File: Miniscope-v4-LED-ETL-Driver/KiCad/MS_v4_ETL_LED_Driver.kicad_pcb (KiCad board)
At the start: 4 copper layers, 8 x 10.5 mm, 20 parts, among them J1 Conn_01x01, J10 Conn_01x05, J6 Conn_01x01, J7 Conn_01x01, U1 MAX14574EWL+, U2 TPL0102-100RUCR, U3 LTC3218

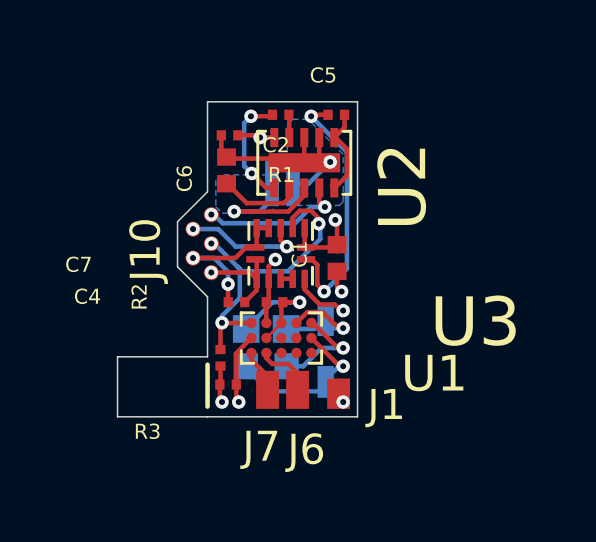
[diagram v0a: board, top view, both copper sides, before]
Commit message: Finalize LED-EWL, MCU, and PYTHON480 PCB for fabrication
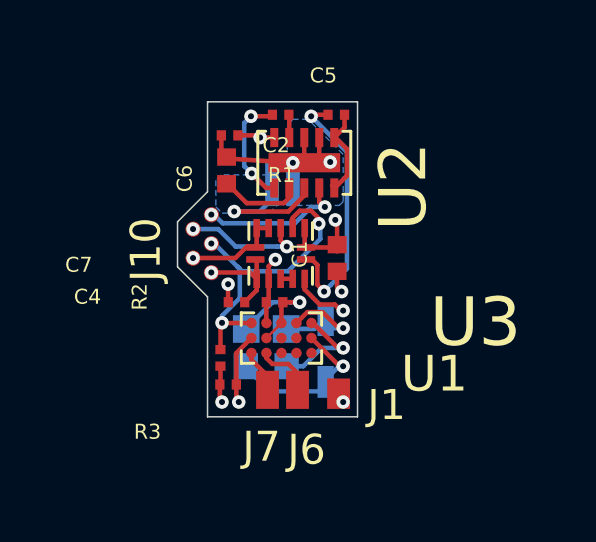
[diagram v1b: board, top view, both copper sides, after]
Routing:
- net GND: track 23.2 -> 22.7 mm, vias 8 -> 9
- added copper zone on In4.Cu, net +3V3
- removed copper zone on In2.Cu, net +3V3
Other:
- board size 8 x 10.5 mm -> 6 x 10.5 mm
- copper layers 4 -> 6
- board text added: "P3"
- board text removed: "P2"
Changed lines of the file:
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@@
-(kicad_pcb (version 20171130) (host pcbnew "(5.0.1)-3")
+(kicad_pcb (version 20171130) (host pcbnew "(5.1.0)-1")
   (general
     (thickness 0.8)
-    (drawings 16)
-    (tracks 211)
+    (drawings 13)
+    (tracks 209)
     (zones 0)
     (modules 20)
@@
     (1 In1.Cu power)
     (2 In2.Cu signal)
+    (3 In3.Cu signal)
+    (4 In4.Cu signal)
     (31 B.Cu signal)
     (32 B.Adhes user)
@@
     (44 Edge.Cuts user)
     (45 Margin user)
-    (46 B.CrtYd user)
-    (47 F.CrtYd user)
+    (46 B.CrtYd user hide)
+    (47 F.CrtYd user hide)
     (48 B.Fab user hide)
     (49 F.Fab user hide)
   )
   (setup
-    (last_trace_width 0.0889)
+    (last_trace_width 0.152)
     (user_trace_width 0.09)
     (user_trace_width 0.1016)
@@
     (zone_45_only yes)
     (trace_min 0.0889)
-    (segment_width 0.2)
-    (edge_width 0.15)
     (via_size 0.45)
     (via_drill 0.2)
@@
     (uvia_min_size 0.2)
     (uvia_min_drill 0.1)
+    (edge_width 0.15)
+    (segment_width 0.2)
     (pcb_text_width 0.3)
     (pcb_text_size 1.5 1.5)
@@
     )
   )
-  (gr_line (start 13.2842 22.0472) (end 13.2842 23.4442) (layer F.SilkS) (width 0.1524))
-  (gr_line (start 10.2842 23.7842) (end 13.2842 23.7842) (layer Edge.Cuts) (width 0.0508))
-  (gr_line (start 10.2842 21.7842) (end 10.2842 23.7842) (layer Edge.Cuts) (width 0.0508))
-  (gr_line (start 13.2842 21.7842) (end 10.2842 21.7842) (layer Edge.Cuts) (width 0.0508))
-  (gr_text P2 (at 15.6718 18.6944) (layer B.SilkS)
+  (gr_line (start 13.2842 21.7842) (end 13.2842 23.7842) (layer Edge.Cuts) (width 0.0508))
+  (gr_text P3 (at 15.6718 18.6944) (layer B.SilkS)
     (effects (font (size 1.5 1.5) (thickness 0.3)) (justify mirror))
   )
@@
   (segment (start 13.97 15.176) (end 13.9192 15.1252) (width 0.152) (layer F.Cu) (net 11))
   (segment (start 16.51 15.3162) (end 16.3698 15.176) (width 0.152) (layer F.Cu) (net 11))
-  (segment (start 16.3698 15.176) (end 13.97 15.176) (width 0.152) (layer F.Cu) (net 11))
+  (segment (start 16.3698 15.176) (end 16.129 15.3162) (width 0.152) (layer F.Cu) (net 11))
   (segment (start 13.7458 14.9518) (end 13.9192 15.1252) (width 0.152) (layer F.Cu) (net 11))
   (segment (start 13.7458 14.4018) (end 13.7458 14.9518) (width 0.152) (layer F.Cu) (net 11))
-  (segment (start 16.6552 16.0092) (end 17.3736 15.2908) (width 0.152) (layer B.Cu) (net 11))
-  (segment (start 16.1342 16.0092) (end 16.6552 16.0092) (width 0.152) (layer B.Cu) (net 11))
   (via (at 17.5425 17.2212) (size 0.45) (drill 0.2) (layers F.Cu B.Cu) (net 11))
   (segment (start 17.6022 18.0462) (end 17.6022 17.2809) (width 0.152) (layer F.Cu) (net 11))
@@
   (segment (start 16.477001 22.098) (end 17.086601 21.4884) (width 0.152) (layer B.Cu) (net 11))
   (segment (start 15.920001 22.098) (end 16.477001 22.098) (width 0.152) (layer B.Cu) (net 11))
-  (segment (start 13.97 18.955546) (end 13.97 19.087402) (width 0.152) (layer B.Cu) (net 11))
-  (segment (start 13.505654 18.4912) (end 13.97 18.955546) (width 0.152) (layer B.Cu) (net 11))
-  (segment (start 12.8016 18.4912) (end 13.505654 18.4912) (width 0.152) (layer B.Cu) (net 11))
   (via (at 13.970001 19.3637) (size 0.45) (drill 0.2) (layers F.Cu B.Cu) (net 11))
-  (segment (start 13.97 19.087402) (end 13.97 19.363699) (width 0.152) (layer B.Cu) (net 11))
   (segment (start 13.97 19.363699) (end 13.970001 19.3637) (width 0.152) (layer B.Cu) (net 11))
   (segment (start 13.970001 19.960001) (end 13.9744 19.9644) (width 0.152) (layer F.Cu) (net 11))
   (segment (start 13.970001 19.3637) (end 13.970001 19.960001) (width 0.152) (layer F.Cu) (net 11))
+  (segment (start 15.494 18.4912) (end 15.5448 18.542) (width 0.152) (layer In1.Cu) (net 11))
+  (segment (start 12.8016 18.4912) (end 15.494 18.4912) (width 0.2032) (layer In1.Cu) (net 11))
+  (segment (start 16.129 15.3162) (end 13.97 15.176) (width 0.152) (layer F.Cu) (net 11))
+  (via (at 16.129 15.3162) (size 0.45) (drill 0.2) (layers F.Cu B.Cu) (net 11))
   (via (at 13.4112 18.9738) (size 0.45) (drill 0.2) (layers F.Cu B.Cu) (net 12))
   (segment (start 14.9226 18.5838) (end 14.8776 18.5388) (width 0.152) (layer F.Cu) (net 12))
@@
     )
   )
-  (zone (net 12) (net_name +3V3) (layer In2.Cu) (hatch full 0.508)
-    (connect_pads yes (clearance 0.254))
-    (min_thickness 0.1524)
-    (fill yes (arc_segments 16) (thermal_gap 1.27) (thermal_bridge_width 0.2794) (smoothing chamfer))
-    (polygon
-      (pts
-        (xy 18.2842 23.7842) (xy 12.2842 23.7842) (xy 12.2842 18.8026) (xy 12.2936 18.8214) (xy 12.2936 23.7744)
-        (xy 13.5382 23.7744) (xy 13.5382 20.0406) (xy 12.2842 18.7866) (xy 12.2842 13.2842) (xy 18.2842 13.2842)
-      )
-    )
-  )
   (zone (net 11) (net_name GND) (layer B.Cu) (hatch full 0.508)
     (connect_pads yes (clearance 0.254))
@@
       )
     )
+  )
+  (zone (net 12) (net_name +3V3) (layer In4.Cu) (hatch full 0.508)
+    (connect_pads yes (clearance 0.254))
+    (min_thickness 0.1524)
+    (fill yes (arc_segments 16) (thermal_gap 1.27) (thermal_bridge_width 0.2794) (smoothing chamfer))
+    (polygon
+      (pts
+        (xy 18.2842 23.7842) (xy 12.2842 23.7842) (xy 12.2842 18.8026) (xy 12.2936 18.8214) (xy 12.2936 23.7744)
+        (xy 13.5382 23.7744) (xy 13.5382 20.0406) (xy 12.2842 18.7866) (xy 12.2842 13.2842) (xy 18.2842 13.2842)
+      )
+    )

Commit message: Add final gerbers and double check layout for fabrication submitted on 05/03/2019
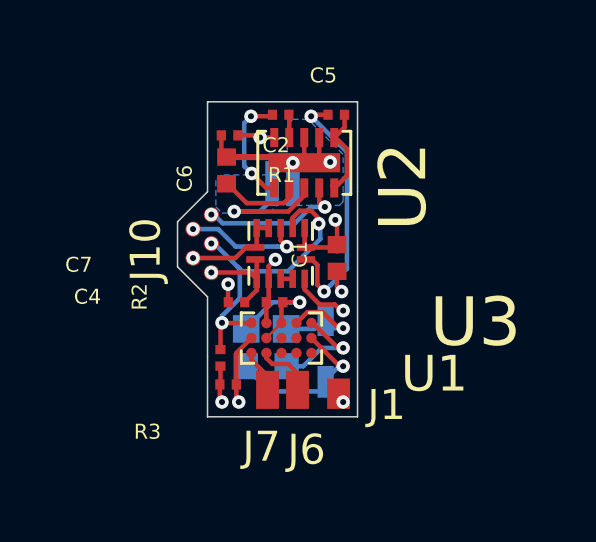
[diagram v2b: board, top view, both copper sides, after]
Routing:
- net GND: track 22.7 -> 23.2 mm
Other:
- rule solder_mask_min_width: 0.25 -> 0.1016
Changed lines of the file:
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@@
     (thickness 0.8)
     (drawings 13)
-    (tracks 209)
+    (tracks 210)
     (zones 0)
     (modules 20)
@@
   )
   (setup
-    (last_trace_width 0.152)
+    (last_trace_width 0.2032)
     (user_trace_width 0.09)
     (user_trace_width 0.1016)
@@
     (pad_drill 0)
     (pad_to_mask_clearance 0.0254)
-    (solder_mask_min_width 0.25)
-    (aux_axis_origin 13.2842 13.2842)
-    (grid_origin 13.2842 13.2842)
+    (solder_mask_min_width 0.1016)
+    (aux_axis_origin 13.2842 23.7842)
+    (grid_origin 13.2842 23.7842)
     (visible_elements 7FFFFFFF)
     (pcbplotparams
       (layerselection 0x010fc_ffffffff)
-      (usegerberextensions false)
+      (usegerberextensions true)
       (usegerberattributes false)
       (usegerberadvancedattributes false)
@@
       (viasonmask false)
       (mode 1)
-      (useauxorigin false)
+      (useauxorigin true)
       (hpglpennumber 1)
       (hpglpenspeed 20)
@@
   (segment (start 15.494 18.4912) (end 15.5448 18.542) (width 0.152) (layer In1.Cu) (net 11))
   (segment (start 12.8016 18.4912) (end 15.494 18.4912) (width 0.2032) (layer In1.Cu) (net 11))
-  (segment (start 16.129 15.3162) (end 13.97 15.176) (width 0.152) (layer F.Cu) (net 11))
   (via (at 16.129 15.3162) (size 0.45) (drill 0.2) (layers F.Cu B.Cu) (net 11))
+  (segment (start 16.319 15.1252) (end 16.51 15.3162) (width 0.2032) (layer F.Cu) (net 11))
+  (segment (start 13.9192 15.1252) (end 16.319 15.1252) (width 0.2032) (layer F.Cu) (net 11))
   (via (at 13.4112 18.9738) (size 0.45) (drill 0.2) (layers F.Cu B.Cu) (net 12))
   (segment (start 14.9226 18.5838) (end 14.8776 18.5388) (width 0.152) (layer F.Cu) (net 12))
